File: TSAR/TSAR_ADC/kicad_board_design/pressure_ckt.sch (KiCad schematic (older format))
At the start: 20 parts, among them U10 MCP3424T-E/ST

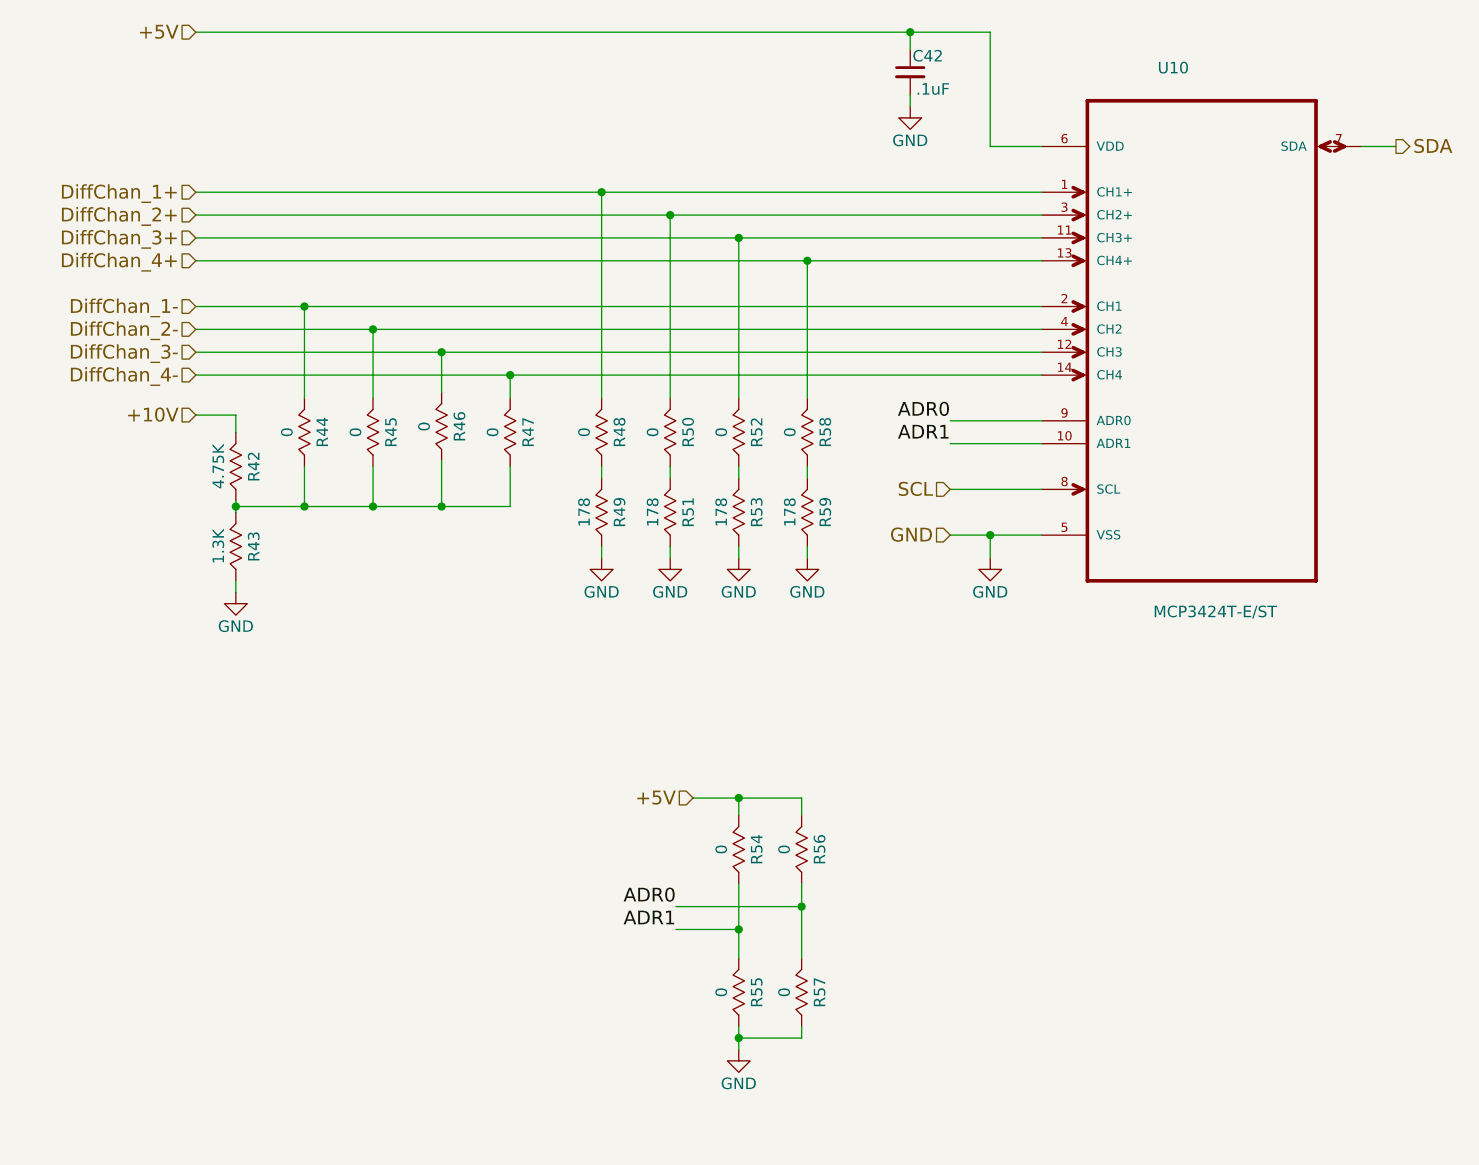
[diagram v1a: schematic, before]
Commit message: Simplify thermocouple signal chain for better worst case.
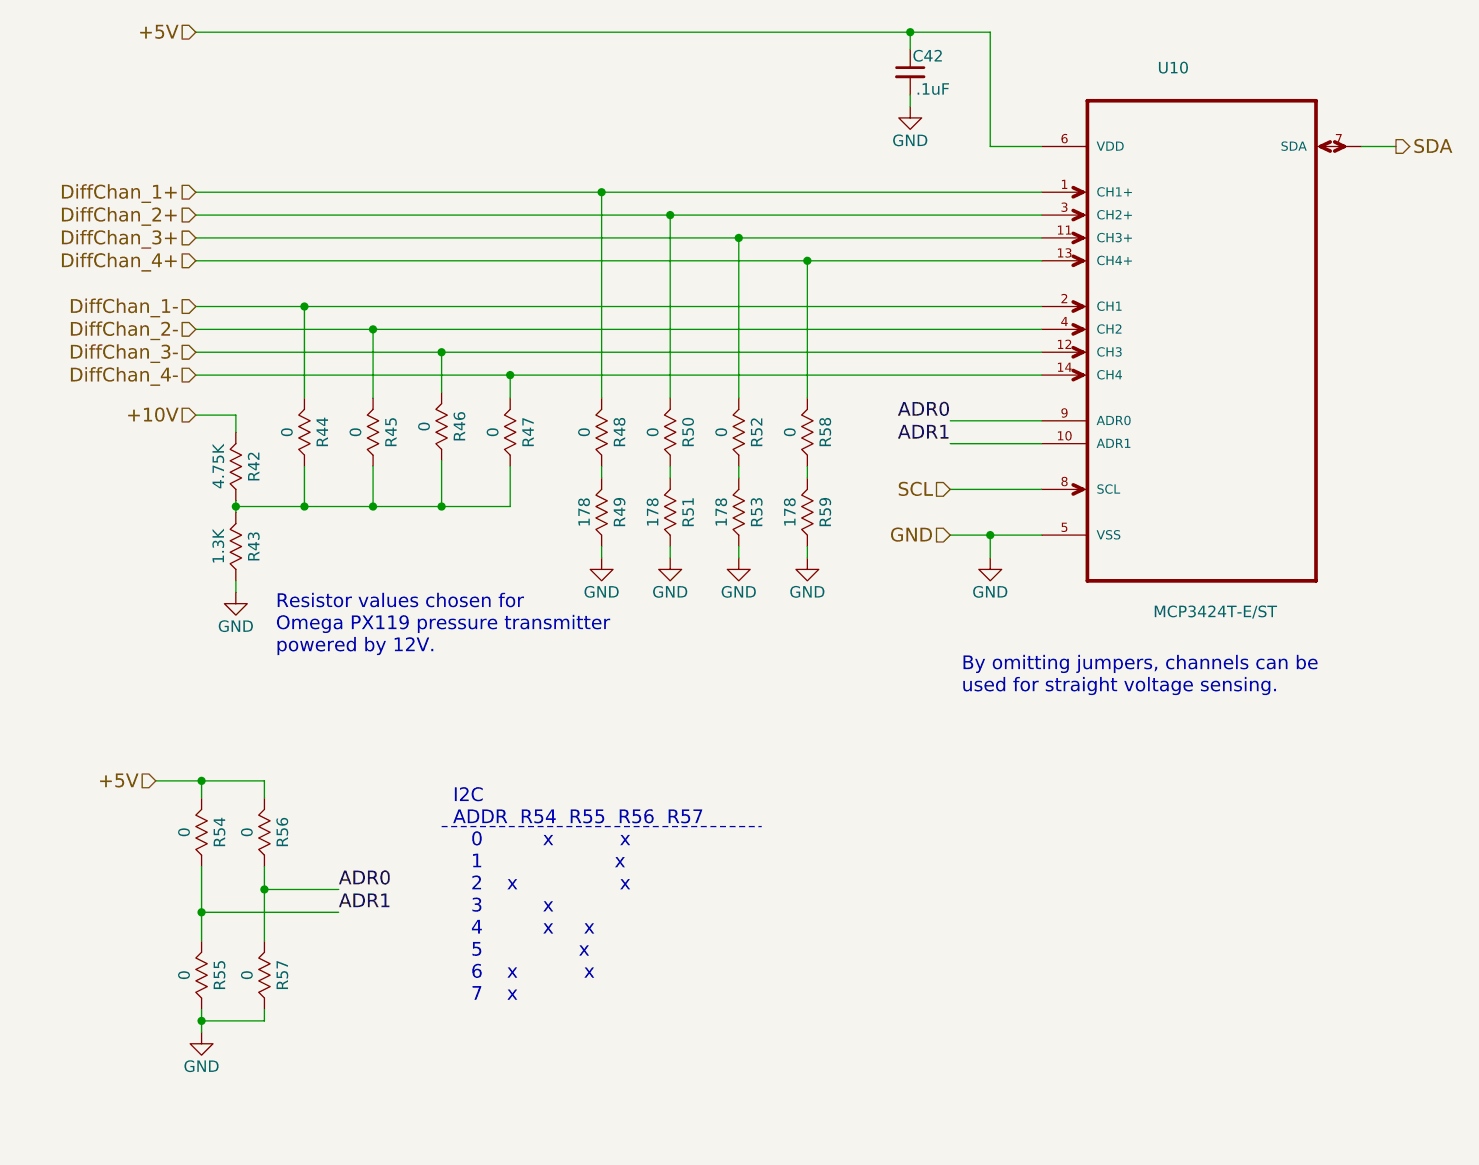
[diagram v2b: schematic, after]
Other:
- note added: "By omitting jumpers, channels can be\nused for straight voltage sensing.\n"
- note added: "I2C\nADDR R54 R55 R56 R57\n 0 x x\n 1 x\n 2 x x\n 3 x\n 4 x x\n 5 x\n 6 x x\n 7 x"
- note added: "Resistor values chosen for \nOmega PX119 pressure transmitter\npowered by 12V."
- moved on the sheet: R54, R55, R56, R57
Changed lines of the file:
@@
 L GND #PWR062
 U 1 1 5B7B5331
-P 5700 6975
-F 0 "#PWR062" H 5700 6725 50  0001 C CNN
-F 1 "GND" H 5700 6825 50  0000 C CNN
-F 2 "" H 5700 6975 50  0000 C CNN
-F 3 "" H 5700 6975 50  0000 C CNN
-	1    5700 6975
+P 3350 6900
+F 0 "#PWR062" H 3350 6650 50  0001 C CNN
+F 1 "GND" H 3350 6750 50  0000 C CNN
+F 2 "" H 3350 6900 50  0000 C CNN
+F 3 "" H 3350 6900 50  0000 C CNN
+	1    3350 6900
 	1    0    0    -1
 $EndComp
@@
 L R R56
 U 1 1 5B8C8610
-P 5975 6100
-F 0 "R56" V 6055 6100 50  0000 C CNN
-F 1 "0" V 5900 6100 50  0000 C CNN
-F 2 "Resistors_SMD:R_0805_HandSoldering" V 5830 6100 50  0001 C CNN
-F 3 "" H 5900 6100 50  0001 C CNN
-F 4 "ERJ-6GEY0R00V" V 5975 6100 60  0001 C CNN "MPN"
-F 5 "Panasonic" V 5975 6100 60  0001 C CNN "MFN"
-F 6 "Digikey" V 5975 6100 60  0001 C CNN "SPR"
-F 7 "P0.0ACT-ND" V 5975 6100 60  0001 C CNN "SPN"
-F 8 "-" H 0   0   50  0001 C CNN "MFR"
-F 9 "-" H 0   0   50  0001 C CNN "SPURL"
-	1    5975 6100
+P 3625 6025
+F 0 "R56" V 3705 6025 50  0000 C CNN
+F 1 "0" V 3550 6025 50  0000 C CNN
+F 2 "Resistors_SMD:R_0805_HandSoldering" V 3480 6025 50  0001 C CNN
+F 3 "" H 3550 6025 50  0001 C CNN
+F 4 "ERJ-6GEY0R00V" V 3625 6025 60  0001 C CNN "MPN"
+F 5 "Panasonic" V 3625 6025 60  0001 C CNN "MFN"
+F 6 "Digikey" V 3625 6025 60  0001 C CNN "SPR"
+F 7 "P0.0ACT-ND" V 3625 6025 60  0001 C CNN "SPN"
+F 8 "-" H -2350 -75 50  0001 C CNN "MFR"
+F 9 "-" H -2350 -75 50  0001 C CNN "SPURL"
+	1    3625 6025
 	1    0    0    -1
 $EndComp
@@
 L R R54
 U 1 1 5B8C86F8
-P 5700 6100
-F 0 "R54" V 5780 6100 50  0000 C CNN
-F 1 "0" V 5625 6100 50  0000 C CNN
-F 2 "Resistors_SMD:R_0805_HandSoldering" V 5555 6100 50  0001 C CNN
-F 3 "" H 5625 6100 50  0001 C CNN
-F 4 "ERJ-6GEY0R00V" V 5700 6100 60  0001 C CNN "MPN"
-F 5 "Panasonic" V 5700 6100 60  0001 C CNN "MFN"
-F 6 "Digikey" V 5700 6100 60  0001 C CNN "SPR"
-F 7 "P0.0ACT-ND" V 5700 6100 60  0001 C CNN "SPN"
-F 8 "-" H 0   0   50  0001 C CNN "MFR"
-F 9 "-" H 0   0   50  0001 C CNN "SPURL"
-	1    5700 6100
+P 3350 6025
+F 0 "R54" V 3430 6025 50  0000 C CNN
+F 1 "0" V 3275 6025 50  0000 C CNN
+F 2 "Resistors_SMD:R_0805_HandSoldering" V 3205 6025 50  0001 C CNN
+F 3 "" H 3275 6025 50  0001 C CNN
+F 4 "ERJ-6GEY0R00V" V 3350 6025 60  0001 C CNN "MPN"
+F 5 "Panasonic" V 3350 6025 60  0001 C CNN "MFN"
+F 6 "Digikey" V 3350 6025 60  0001 C CNN "SPR"
+F 7 "P0.0ACT-ND" V 3350 6025 60  0001 C CNN "SPN"
+F 8 "-" H -2350 -75 50  0001 C CNN "MFR"
+F 9 "-" H -2350 -75 50  0001 C CNN "SPURL"
+	1    3350 6025
 	1    0    0    -1
 $EndComp
@@
 L R R55
 U 1 1 5B8C8758
-P 5700 6725
-F 0 "R55" V 5780 6725 50  0000 C CNN
-F 1 "0" V 5625 6725 50  0000 C CNN
-F 2 "Resistors_SMD:R_0805_HandSoldering" V 5555 6725 50  0001 C CNN
-F 3 "" H 5625 6725 50  0001 C CNN
-F 4 "ERJ-6GEY0R00V" V 5700 6725 60  0001 C CNN "MPN"
-F 5 "Panasonic" V 5700 6725 60  0001 C CNN "MFN"
-F 6 "Digikey" V 5700 6725 60  0001 C CNN "SPR"
-F 7 "P0.0ACT-ND" V 5700 6725 60  0001 C CNN "SPN"
-F 8 "-" H 0   0   50  0001 C CNN "MFR"
-F 9 "-" H 0   0   50  0001 C CNN "SPURL"
-	1    5700 6725
+P 3350 6650
+F 0 "R55" V 3430 6650 50  0000 C CNN
+F 1 "0" V 3275 6650 50  0000 C CNN
+F 2 "Resistors_SMD:R_0805_HandSoldering" V 3205 6650 50  0001 C CNN
+F 3 "" H 3275 6650 50  0001 C CNN
+F 4 "ERJ-6GEY0R00V" V 3350 6650 60  0001 C CNN "MPN"
+F 5 "Panasonic" V 3350 6650 60  0001 C CNN "MFN"
+F 6 "Digikey" V 3350 6650 60  0001 C CNN "SPR"
+F 7 "P0.0ACT-ND" V 3350 6650 60  0001 C CNN "SPN"
+F 8 "-" H -2350 -75 50  0001 C CNN "MFR"
+F 9 "-" H -2350 -75 50  0001 C CNN "SPURL"
+	1    3350 6650
 	1    0    0    -1
 $EndComp
@@
 L R R57
 U 1 1 5B8C87E9
-P 5975 6725
-F 0 "R57" V 6055 6725 50  0000 C CNN
-F 1 "0" V 5900 6725 50  0000 C CNN
-F 2 "Resistors_SMD:R_0805_HandSoldering" V 5830 6725 50  0001 C CNN
-F 3 "" H 5900 6725 50  0001 C CNN
-F 4 "ERJ-6GEY0R00V" V 5975 6725 60  0001 C CNN "MPN"
-F 5 "Panasonic" V 5975 6725 60  0001 C CNN "MFN"
-F 6 "Digikey" V 5975 6725 60  0001 C CNN "SPR"
-F 7 "P0.0ACT-ND" V 5975 6725 60  0001 C CNN "SPN"
-F 8 "-" H 0   0   50  0001 C CNN "MFR"
-F 9 "-" H 0   0   50  0001 C CNN "SPURL"
-	1    5975 6725
+P 3625 6650
+F 0 "R57" V 3705 6650 50  0000 C CNN
+F 1 "0" V 3550 6650 50  0000 C CNN
+F 2 "Resistors_SMD:R_0805_HandSoldering" V 3480 6650 50  0001 C CNN
+F 3 "" H 3550 6650 50  0001 C CNN
+F 4 "ERJ-6GEY0R00V" V 3625 6650 60  0001 C CNN "MPN"
+F 5 "Panasonic" V 3625 6650 60  0001 C CNN "MFN"
+F 6 "Digikey" V 3625 6650 60  0001 C CNN "SPR"
+F 7 "P0.0ACT-ND" V 3625 6650 60  0001 C CNN "SPN"
+F 8 "-" H -2350 -75 50  0001 C CNN "MFR"
+F 9 "-" H -2350 -75 50  0001 C CNN "SPURL"
+	1    3625 6650
 	1    0    0    -1
 $EndComp
@@
 Text HLabel 3325 4200 0    60   Input ~ 0
 +10V
-Text Label 5425 6350 2    60   ~ 0
+Text Label 3950 6275 0    60   ~ 0
 ADR0
-Text Label 5425 6450 2    60   ~ 0
+Text Label 3950 6375 0    60   ~ 0
 ADR1
-Text HLabel 5500 5875 0    60   Input ~ 0
+Text HLabel 3150 5800 0    60   Input ~ 0
 +5V
 Text Label 6625 4225 2    60   ~ 0
@@
 ADR1
 Wire Wire Line
-	6625 4725 7025 4725
+	6625 4725 6800 4725
+Wire Wire Line
+	6800 4725 7025 4725
 Wire Wire Line
 	6800 4725 6800 4825
@@
 	8425 3025 8575 3025
 Wire Wire Line
-	3325 3225 7025 3225
-Wire Wire Line
-	3325 3325 7025 3325
-Wire Wire Line
-	3325 3425 7025 3425
-Wire Wire Line
-	3325 3525 7025 3525
-Wire Wire Line
-	3325 3725 7025 3725
-Wire Wire Line
-	3325 3825 7025 3825
-Wire Wire Line
-	3325 3925 7025 3925
-Wire Wire Line
-	3325 4025 7025 4025
+	3325 3225 5100 3225
+Wire Wire Line
+	5100 3225 7025 3225
+Wire Wire Line
+	3325 3325 5400 3325
+Wire Wire Line
+	5400 3325 7025 3325
+Wire Wire Line
+	3325 3425 5700 3425
+Wire Wire Line
+	5700 3425 7025 3425
+Wire Wire Line
+	3325 3525 6000 3525
+Wire Wire Line
+	6000 3525 7025 3525
+Wire Wire Line
+	3325 3725 3800 3725
+Wire Wire Line
+	3800 3725 7025 3725
+Wire Wire Line
+	3325 3825 4100 3825
+Wire Wire Line
+	4100 3825 7025 3825
+Wire Wire Line
+	3325 3925 4400 3925
+Wire Wire Line
+	4400 3925 7025 3925
+Wire Wire Line
+	3325 4025 4700 4025
+Wire Wire Line
+	4700 4025 7025 4025
 Wire Wire Line
 	5100 4825 5100 4775
@@
 	3500 4975 3500 4925
 Wire Wire Line
-	3500 4575 3500 4625
+	3500 4575 3500 4600
+Wire Wire Line
+	3500 4600 3500 4625
 Wire Wire Line
 	3325 4200 3500 4200
@@
 	3500 4200 3500 4275
 Wire Wire Line
-	3500 4600 4700 4600
-Wire Wire Line
-	5500 5875 5975 5875
-Wire Wire Line
-	5700 5875 5700 5950
-Wire Wire Line
-	5975 5875 5975 5950
-Wire Wire Line
-	5700 6250 5700 6575
-Wire Wire Line
-	5700 6450 5425 6450
-Wire Wire Line
-	5425 6350 5975 6350
-Wire Wire Line
-	5975 6250 5975 6575
+	3500 4600 3800 4600
+Wire Wire Line
+	3800 4600 4100 4600
+Wire Wire Line
+	4100 4600 4400 4600
+Wire Wire Line
+	4400 4600 4700 4600
+Wire Wire Line
+	3150 5800 3350 5800
+Wire Wire Line
+	3350 5800 3625 5800
+Wire Wire Line
+	3350 5800 3350 5875
+Wire Wire Line
+	3625 5800 3625 5875
+Wire Wire Line
+	3350 6175 3350 6375
+Wire Wire Line
+	3350 6375 3350 6500
+Wire Wire Line
+	3625 6175 3625 6275
+Wire Wire Line
+	3625 6275 3625 6500
 Wire Wire Line
 	6450 2850 6450 2800
@@
 	6800 3025 6800 2525
 Wire Wire Line
-	6800 2525 3325 2525
+	6800 2525 6450 2525
+Wire Wire Line
+	6450 2525 3325 2525
 Wire Wire Line
 	6450 2525 6450 2600
@@
 Connection ~ 4100 4600
 Connection ~ 3800 4600
-Connection ~ 5700 5875
-Connection ~ 5700 6450
-Connection ~ 5975 6350
+Connection ~ 3350 5800
+Connection ~ 3350 6375
+Connection ~ 3625 6275
 Connection ~ 6450 2525
 Wire Wire Line
 	4400 4400 4400 4600
 Wire Wire Line
-	5975 6875 5975 6925
-Wire Wire Line
-	5975 6925 5700 6925
-Wire Wire Line
-	5700 6875 5700 6975
-Connection ~ 5700 6925
+	3625 6800 3625 6850
+Wire Wire Line
+	3625 6850 3350 6850
+Wire Wire Line
+	3350 6800 3350 6850
+Wire Wire Line
+	3350 6850 3350 6900
+Connection ~ 3350 6850
+Text Notes 3675 5250 0    60   ~ 0
+Resistor values chosen for \nOmega PX119 pressure transmitter\npowered by 12V.
+Text Notes 6675 5425 0    60   ~ 0
+By omitting jumpers, channels can be\nused for straight voltage sensing.\n
+Text Notes 4450 6775 0    60   ~ 0
+ I2C\nADDR  R54  R55  R56  R57\n   0          x           x\n   1                      x\n   2    x                 x\n   3          x\n   4          x     x\n   5                x\n   6    x           x\n   7    x
+Wire Notes Line
+	4400 6000 5800 6000
+Wire Wire Line
+	3625 6275 3950 6275
+Wire Wire Line
+	3350 6375 3950 6375
 $EndSCHEMATC
